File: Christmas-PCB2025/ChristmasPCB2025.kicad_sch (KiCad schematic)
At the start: 29 parts, among them J2 Conn_01x08, Q2 2N7002_C306856, U1 AMS1117-3.3_C347222, U4 ESP32-C3_SUPERMINI_TH

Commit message: removed many unnecessary components
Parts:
- removed C1: 47uF 10V, Capacitor_SMD:C_1210_3225Metric_Pad1.33x2.70mm_HandSolder, symbol Device:C_Small
- removed D3: 1N5819_C437199, easyeda2kicad:SMA_L4.4-W2.6-LS5.0-RD, symbol easyeda2kicad:1N5819_C437199
- removed R3, R4: 5k1, Resistor_SMD:R_1206_3216Metric_Pad1.30x1.75mm_HandSolder, symbol Device:R
- removed U1: AMS1117-3.3_C347222, easyeda2kicad:SOT-223-4_L6.5-W3.5-P2.30-LS7.0-BR, symbol easyeda2kicad:AMS1117-3.3_C347222
- removed USB1: TYPE-C 6P(073), easyeda2kicad:TYPE-C-SMD_TYPE-C-6P_5, symbol easyeda2kicad:TYPE-C6P(073)
- added BATT+1: ~, TestPoint:TestPoint_Pad_D3.0mm, symbol Connector:TestPoint_Alt
- added BATT-1: TestPoint_Alt, TestPoint:TestPoint_Pad_D3.0mm, symbol Connector:TestPoint_Alt
- added BATTPACK1: Batteryplaceholder, MountingHole:MountingHole_2.1mm, symbol Mechanical:MountingHole
- added D1: 1N5819_C437199, easyeda2kicad:SMA_L4.4-W2.6-LS5.0-RD, symbol easyeda2kicad:1N5819_C437199
- added D6: SM712_SOT23, Package_TO_SOT_SMD:SOT-23, symbol Diode:SM712_SOT23
- added R1, R2: 10k, Resistor_SMD:R_1206_3216Metric_Pad1.30x1.75mm_HandSolder, symbol Device:R_Small
- F1: value Fuse_Small 2A -> Resetable fuse 0.75A
- J1: renamed from J2; footprint Connector_PinHeader_2.54mm:PinHeader_1x08_P2.54mm_Vertical -> Connector_PinHeader_2.54mm:PinHeader_1x08_P2.54mm_Vertical_SMD_Pin1Left
- R7: renamed from R20; value 200 -> 100
- renumbered KEY3 to BUTTON1, KEY4 to BUTTON2, D25 to D10, D16 to D2, D17 to D3, D18 to D4, D19 to D5, D22 to D7, D23 to D8, D24 to D9, JP2 to JP1, LS2 to LS1, Q2 to Q1, R2 to R3, R17 to R4, R13 to R5, R10 to R6, U4 to U1
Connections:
- net GND: now also BATT-1.1, D6.3 (common), R2.2
- net SCL: now also D6.1 (A1)
- net SDA: now also D6.2 (A2)
- net at BT1.1: now also BATT+1.1, D1.2 (A), R1.1
- net at F1.2: now also D1.1 (C)
- net BATT_V: now reaches U1.0 (GPIO0)
- net BATT_V: now also R1.2, R2.1
- no-connect marks 8 -> 7
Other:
- note added: "Battery Power"
- note added: "ESD protection"
- note added: "GPIO header"
- note added: "Microcontroller"
- note added: "Populate with either 2*CR2032 OR 3/4*AAA Battery holders"
- note added: "RGB LEDs"
- note removed: "Populate with either 2*CR2032 OR 3*AAA Battery holders"
- note removed: "RGBs"
- note removed: "USB-C (Power only)"
- title: Kinderdorp Printplaat -> Christmas_PCB

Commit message: added new design types
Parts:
- removed D10, D2, D3, D4, D5, D7, D8, D9: WS2812B, easyeda2kicad:LED-SMD_4P-L5.0-W5.0-BL_TC5050RGB, symbol LED:WS2812B
- added LED1, LED2, LED3, LED4, LED5, LED6, LED7, LED8: WS2812B, easyeda2kicad:LED-SMD_4P-L5.0-W5.0-BL_TC5050RGB, symbol LED:WS2812B
- renumbered D6 to D1, R3 to LDR1, R2 to R1, R1 to R2, R5 to R3, R6 to R4, R7 to R5, R4 to R7
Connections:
- net +5V: now also LED1.1 (VDD), LED2.1 (VDD), LED3.1 (VDD), LED4.1 (VDD), LED5.1 (VDD), LED6.1 (VDD), LED7.1 (VDD), LED8.1 (VDD)
- net GND: now also LED1.3 (VSS), LED2.3 (VSS), LED3.3 (VSS), LED4.3 (VSS), LED5.3 (VSS), LED6.3 (VSS), LED7.3 (VSS), LED8.3 (VSS)
- net at R3.1: now also LED1.4 (DIN)
- new net: LED1.2 (DOUT), LED2.4 (DIN)
- new net: LED3.2 (DOUT), LED4.4 (DIN)
- new net: LED2.2 (DOUT), LED3.4 (DIN)
- new net: LED5.2 (DOUT), LED6.4 (DIN)
- new net: LED4.2 (DOUT), LED5.4 (DIN)
- new net: LED7.2 (DOUT), LED8.4 (DIN)
- new net: LED6.2 (DOUT), LED7.4 (DIN)

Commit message: settled on ornament design
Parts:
- renumbered D1 to D2
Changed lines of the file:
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@@
 		(dnp no)
 		(fields_autoplaced yes)
-		(property "Reference" "D1"
+		(property "Reference" "D2"
 			(at 217.17 38.1 0)
 			(effects
@@
 			(project "ChristmasPCB2025"
 				(path "/17f7643f-a16b-4802-8051-c0810a7f40c9"
-					(reference "D1")
+					(reference "D2")
 					(unit 1)
 				)

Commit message: finished playfull routing
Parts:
- removed D2: SM712_SOT23, Package_TO_SOT_SMD:SOT-23, symbol Diode:SM712_SOT23
- removed J1: Conn_01x08, Connector_PinHeader_2.54mm:PinHeader_1x08_P2.54mm_Vertical_SMD_Pin1Left, symbol Connector_Generic:Conn_01x08
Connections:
- net RGB: now also U1.3 (GPIO3)
- net INT: no longer names the net of U1.20 (GPIO20)
- net SCL: no longer names the net of JP1.2 (B), U1.9 (GPIO9)
- net SDA: no longer names the net of U1.8 (GPIO8)
- net SDO: no longer names the net of U1.21 (GPIO21)
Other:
- note removed: "ESD protection"
- note removed: "GPIO header"

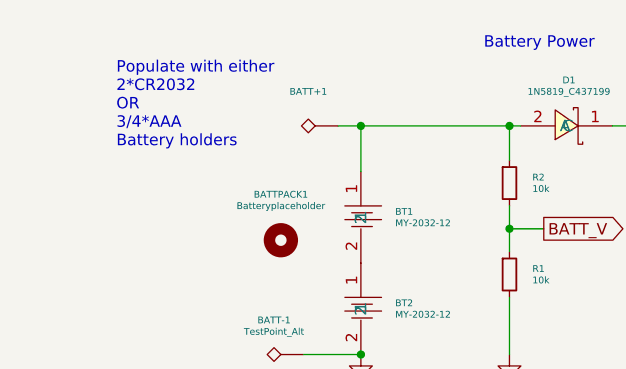
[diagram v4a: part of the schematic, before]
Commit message: fixed documentation error
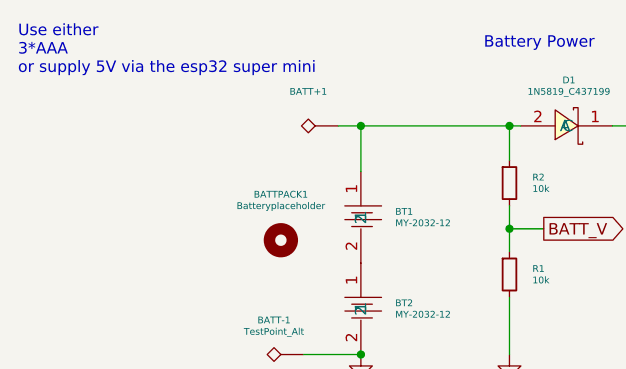
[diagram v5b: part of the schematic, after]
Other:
- note added: "Use either 3*AAA or supply 5V via the esp32 super mini"
- note removed: "Populate with either 2*CR2032 OR 3/4*AAA Battery holders"
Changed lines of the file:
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@@
 		(comment 1 "Casper R. Tak")
 	)
-	(text "Populate with either\n2*CR2032\nOR\n3/4*AAA\nBattery holders"
+	(text "Use either\n3*AAA\nor supply 5V via the esp32 super mini"
 		(exclude_from_sim no)
-		(at 29.972 45.974 0)
+		(at 19.05 39.878 0)
 		(effects
 			(font

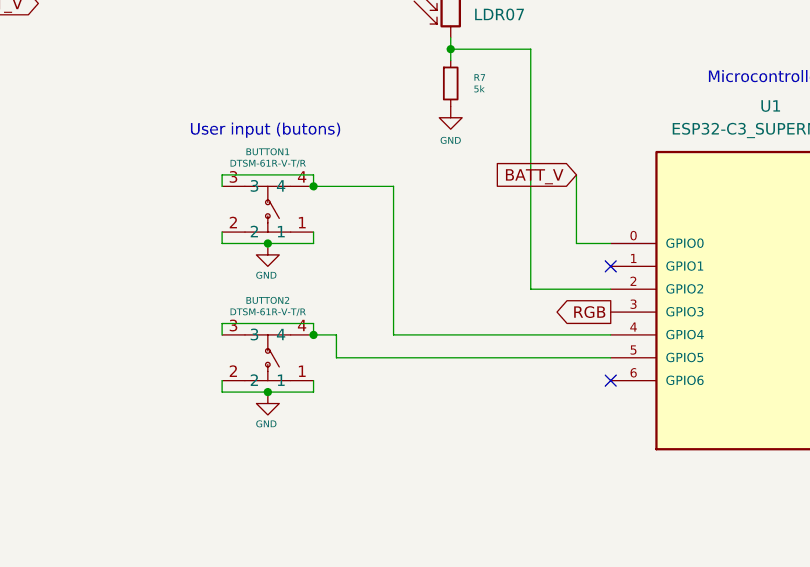
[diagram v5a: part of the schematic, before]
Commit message: working on code and fixed button design error.
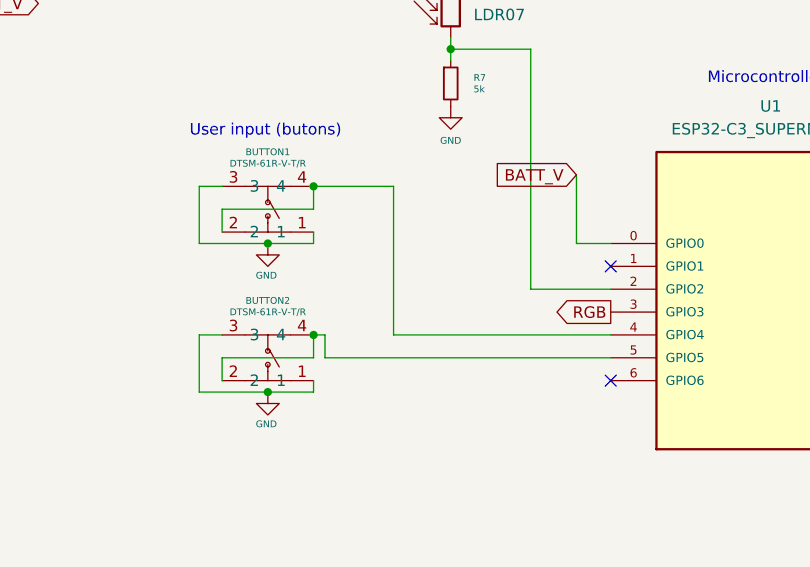
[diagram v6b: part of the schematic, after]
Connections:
- net GND: now also BUTTON1.3, BUTTON2.3; no longer BUTTON1.2, BUTTON2.2
- net at BUTTON2.4, U1.5 (GPIO5): now also BUTTON2.2; no longer BUTTON2.3
- net at BUTTON1.4, U1.4 (GPIO4): now also BUTTON1.2; no longer BUTTON1.3
